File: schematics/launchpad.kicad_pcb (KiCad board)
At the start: 2 copper layers, 19 parts, among them J1 Conn_01x05_Female, U1 74HC595, U2 74HC595, U3 74HC595, U4 74HC595, U5 74HC595

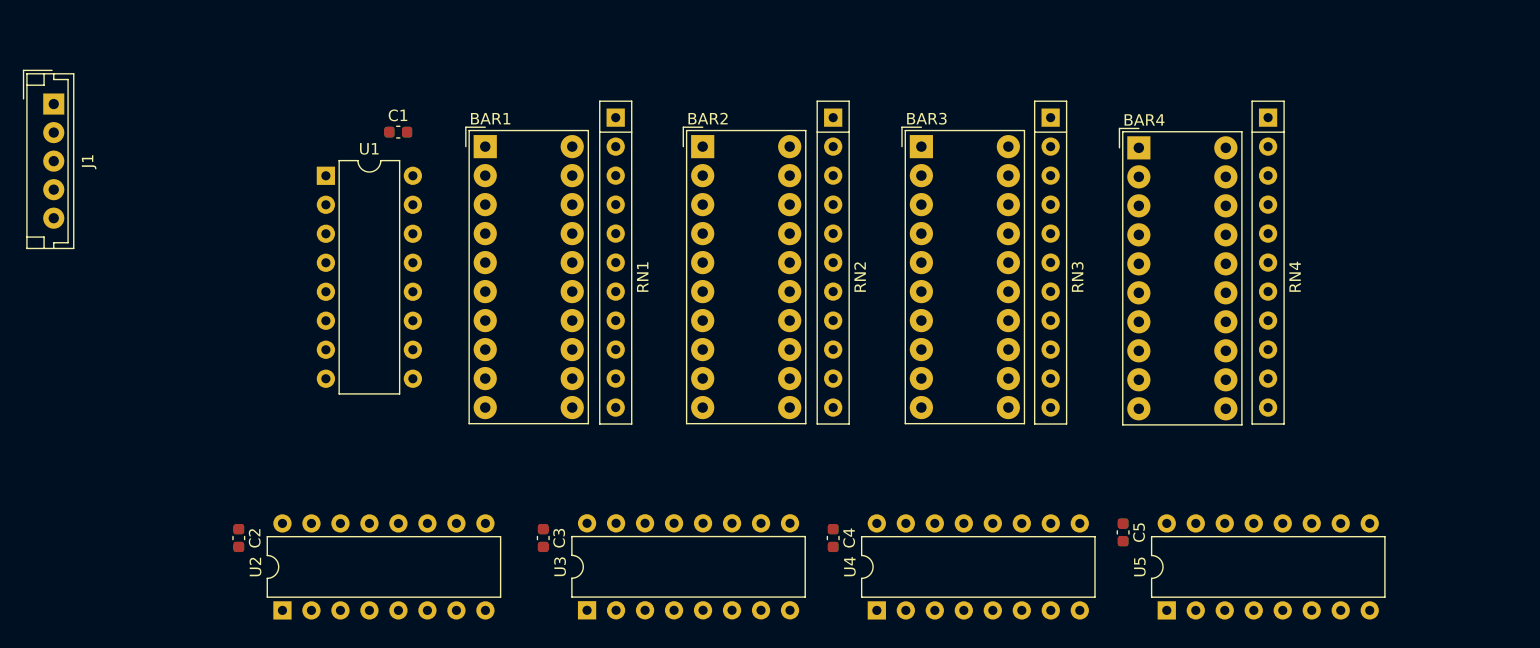
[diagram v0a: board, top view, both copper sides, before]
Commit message: SCH: Gauges routing complete
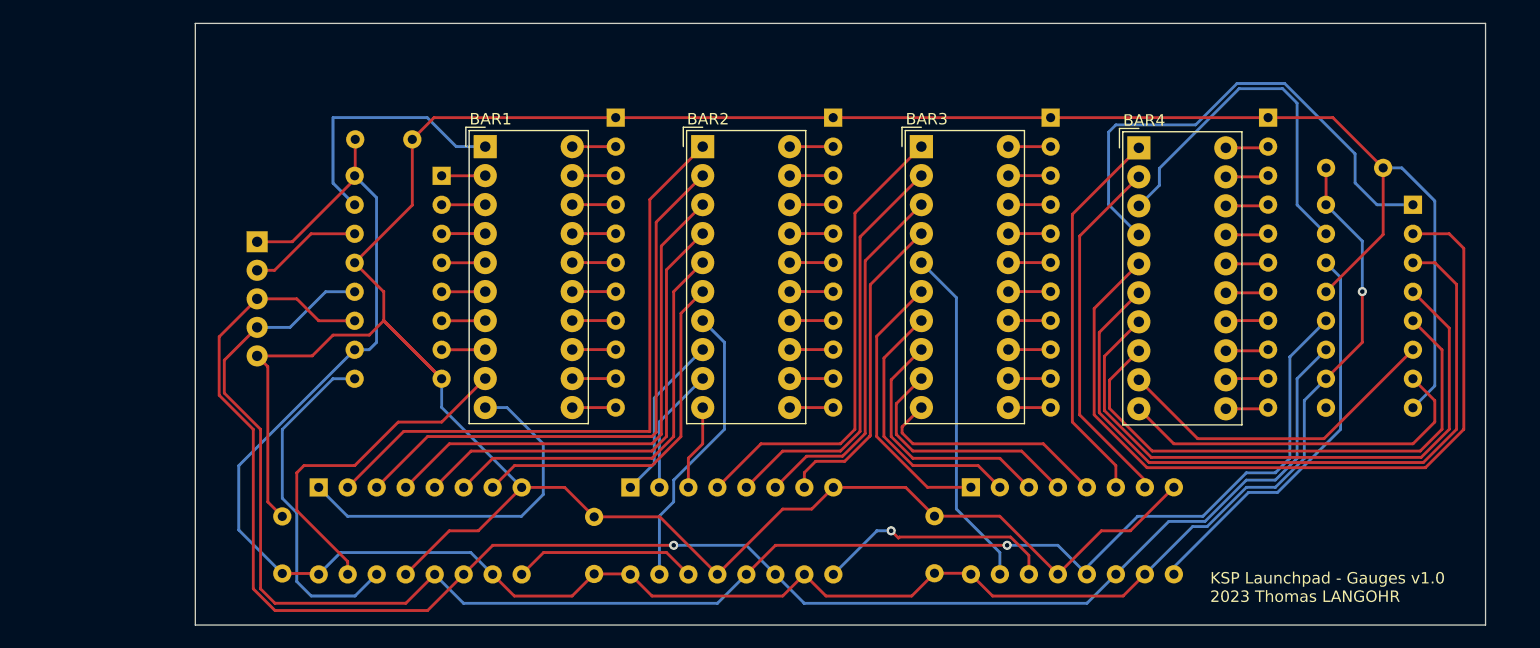
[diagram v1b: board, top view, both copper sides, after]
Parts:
- C1, C2, C3, C4, C5: footprint Capacitor_SMD:C_0603_1608Metric -> Capacitor_THT:C_Disc_D4.3mm_W1.9mm_P5.00mm; moved to B.Cu
- J1, RN1, RN2, RN3, RN4, U1, U2, U3, U4, U5: moved to B.Cu
- moved U4 58.9 mm to (-375.9, 44.5), turned to 180 degrees
- moved C5 36.5 mm to (-383.5, 41.2), turned to 0 degrees
- moved J1 21.5 mm to (-477.2, 47.7)
- moved U5 20.3 mm to (-414.7, 69.2), turned to -90 degrees
- moved U3 11.4 mm to (-444.5, 69.2), turned to -90 degrees
- moved U2 11.2 mm to (-471.8, 69.2), turned to -90 degrees
- moved U1 10.1 mm to (-461.0, 41.9), turned to 180 degrees
- moved C4 9.40 mm to (-417.8, 76.7), turned to 90 degrees
- moved C3 5.46 mm to (-447.7, 76.8), turned to 90 degrees
- moved C2 4.91 mm to (-475.0, 76.8), turned to 90 degrees
- moved C1 3.82 mm to (-468.6, 38.7)
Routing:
- net GND: track 0.00 -> 281.5 mm
- net +5V: track 0.00 -> 187.9 mm, vias 0 -> 1
- net /DG_CLK: track 0.00 -> 149.9 mm, vias 0 -> 1
- net /~{DG_LATCH}: track 0.00 -> 149.1 mm, vias 0 -> 1
- net Net-(U4-QC): track 0.00 -> 71.4 mm
- net Net-(U4-QD): track 0.00 -> 63.6 mm
- net Net-(U2-QC): track 0.00 -> 55.4 mm
- net Net-(U4-QE): track 0.00 -> 55.3 mm
- net Net-(U2-QD): track 0.00 -> 50.7 mm
- net Net-(U4-QF): track 0.00 -> 48.1 mm
- net Net-(U2-QE): track 0.00 -> 46.0 mm
- net Net-(U4-QB): track 0.00 -> 44.4 mm
- net Net-(U3-QE): track 0.00 -> 41.3 mm
- net Net-(U2-QF): track 0.00 -> 41.2 mm
- net Net-(U3-QF): track 0.00 -> 36.6 mm
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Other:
- board outline added: 113 x 52.7 mm
- board text added: "KSP Launchpad - Gauges v1.0 2023 Thomas LANGOHR"

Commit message: SCH: routing improvement
+ground plane
+via stiching
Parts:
- added REF**: OSHW-Symbol_6.7x6mm_SilkScreen, Symbol:OSHW-Symbol_6.7x6mm_SilkScreen, F.Cu at (202.2, 75.7)
- added REF**: OSHW-Symbol_6.7x6mm_SilkScreen, Symbol:OSHW-Symbol_6.7x6mm_SilkScreen, B.Cu at (202.2, 75.7)
- BAR1: value HDSP-4832_2 -> GCBDX10D
- BAR2: value HDSP-4832_2 -> XGUYX10D
- BAR3: value HDSP-4832_2 -> XGMRX10D
- BAR4: value HDSP-4832_2 -> XGUGX10D
- U1, U2, U3, U4, U5: value 74HC595 -> 74HC595N
- moved BAR1 578.8 mm to (120.2, 79.0)
- moved BAR2 578.8 mm to (139.3, 79.0)
- moved BAR3 578.8 mm to (158.4, 79.0)
- moved BAR4 578.8 mm to (177.5, 79.1)
- moved C1 578.8 mm to (108.8, 78.3)
- moved C2 578.8 mm to (102.4, 116.4)
- moved C3 578.8 mm to (129.8, 116.4)
- moved C4 578.8 mm to (159.6, 116.3)
- moved C5 578.8 mm to (193.9, 80.8)
- moved J1 578.8 mm to (100.2, 87.3)
- moved RN1 578.8 mm to (131.7, 76.4)
- moved RN2 578.8 mm to (150.7, 76.4)
- moved RN3 578.8 mm to (169.8, 76.4)
- moved RN4 578.8 mm to (188.8, 76.4)
- moved U1 578.8 mm to (116.4, 81.5)
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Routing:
- net GND: track 281.5 -> 1.90 mm, vias 0 -> 1
- net +5V: track 187.9 -> 184.2 mm, vias 1 -> 0
- net Net-(U4-QC): track 71.4 -> 68.2 mm
- net Net-(U3-QH'): track 21.4 -> 18.3 mm, vias 1 -> 0
- net Net-(U4-QD): track 63.6 -> 60.9 mm
- net Net-(U4-QG): track 29.4 -> 31.7 mm
- net Net-(U4-SER): track 35.4 -> 37.2 mm
- net /DG_CLK: track 149.9 -> 148.1 mm
- net Net-(U4-QB): track 44.4 -> 42.8 mm
- net Net-(U2-QA): track 30.7 -> 32.2 mm
- net Net-(U4-QA): track 32.0 -> 33.5 mm
- net Net-(U4-QE): track 55.3 -> 54.0 mm
- net Net-(U4-QF): track 48.1 -> 46.8 mm
- net Net-(U5-QH): track 31.7 -> 30.7 mm
- net Net-(U3-QA): track 25.4 -> 26.3 mm
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- added copper zone on F.Cu, net (none)
- added copper zone on B.Cu, net GND
- added copper zone on F.Cu, net GND
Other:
- board size 113 x 52.7 mm -> 116 x 53.9 mm
- board text added: "{ "ViaStitching": "0.1", "stitch_zone_1": { "HSpacing": "2.2", "VSpacing": "2.2", "Clearance": "2", "Randomize": false } }"
